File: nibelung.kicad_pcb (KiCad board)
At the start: 2 copper layers, 0 parts

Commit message: Begin preliminary placement
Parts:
- added C1: 0.1uF, Capacitor_SMD:C_0805_2012Metric_Pad1.18x1.45mm_HandSolder, F.Cu at (111.8, 48.3)
- added C2: 10uF, Capacitor_SMD:C_0805_2012Metric_Pad1.18x1.45mm_HandSolder, F.Cu at (87.8, 77.3)
- added C3: 0.1uF, Capacitor_SMD:C_0805_2012Metric_Pad1.18x1.45mm_HandSolder, F.Cu at (116.6, 45.2)
- added C4: 10uF, Capacitor_SMD:C_0805_2012Metric_Pad1.18x1.45mm_HandSolder, F.Cu at (91.6, 72.8)
- added C5: 47nF, Capacitor_SMD:C_0805_2012Metric_Pad1.18x1.45mm_HandSolder, F.Cu at (111.8, 45.2)
- added C6: 10uF, Capacitor_SMD:C_0805_2012Metric_Pad1.18x1.45mm_HandSolder, F.Cu at (60.5, 82.1)
- added C7: 47nF, Capacitor_SMD:C_0805_2012Metric_Pad1.18x1.45mm_HandSolder, F.Cu at (55.7, 82.1)
- added C8: 0.1uF, Capacitor_SMD:C_0805_2012Metric_Pad1.18x1.45mm_HandSolder, F.Cu at (50.9, 82.1)
- added H1: M2, MountingHole:MountingHole_2.2mm_M2, F.Cu at (70.5, 79.1)
- added H2: M2, MountingHole:MountingHole_2.2mm_M2, F.Cu at (76.5, 79.1)
- added H3: M2, MountingHole:MountingHole_2.2mm_M2, F.Cu at (82.4, 79.1)
- added H4: M2, MountingHole:MountingHole_2.2mm_M2, F.Cu at (86.2, 72.9)
- added J2: AudioJack3-TSW, Connector_Audio:Jack_3.5mm_CUI_SJ-3524-SMT_Horizontal, F.Cu at (109.0, 101.6)
- added J3: ScrewTerm_01x08_3.5mm, nibelung:TerminalBlock_Molex_393570008_1x08_P3.50mm_Horizontal, F.Cu at (108.4, 114.6)
- added J4: ScrewTerm_01x08_3.5mm, nibelung:TerminalBlock_Molex_393570008_1x08_P3.50mm_Horizontal, F.Cu at (132.9, 88.6)
- added J5: JST_SH_01x04, Connector_JST:JST_SH_SM04B-SRSS-TB_1x04-1MP_P1.00mm_Horizontal, F.Cu at (135.3, 101.6)
- added J6: JST_SH_01x03, Connector_JST:JST_SH_SM03B-SRSS-TB_1x03-1MP_P1.00mm_Horizontal, B.Cu at (135.3, 104.8)
- added J7: JST_SH_01x03, Connector_JST:JST_SH_SM03B-SRSS-TB_1x03-1MP_P1.00mm_Horizontal, B.Cu at (135.3, 98.4)
- added JP1: SJ2, Jumper:SolderJumper-2_P1.3mm_Bridged_Pad1.0x1.5mm, F.Cu at (111.5, 63.3)
- added JP2: SJ2, Jumper:SolderJumper-2_P1.3mm_Bridged_Pad1.0x1.5mm, F.Cu at (106.5, 70.1)
- added R1: 100, Resistor_SMD:R_0805_2012Metric_Pad1.20x1.40mm_HandSolder, F.Cu at (116.5, 48.2)
- added R10: 100, Resistor_SMD:R_0805_2012Metric_Pad1.20x1.40mm_HandSolder, F.Cu at (116.5, 54.2)
- added R11: 100, Resistor_SMD:R_0805_2012Metric_Pad1.20x1.40mm_HandSolder, F.Cu at (101.9, 66.9)
- added R12: 100, Resistor_SMD:R_0805_2012Metric_Pad1.20x1.40mm_HandSolder, F.Cu at (106.7, 66.9)
- added R13: 100, Resistor_SMD:R_0805_2012Metric_Pad1.20x1.40mm_HandSolder, F.Cu at (97.3, 75.8)
- added R14: 100, Resistor_SMD:R_0805_2012Metric_Pad1.20x1.40mm_HandSolder, F.Cu at (111.7, 60.1)
- added R15: 100, Resistor_SMD:R_0805_2012Metric_Pad1.20x1.40mm_HandSolder, F.Cu at (101.1, 72.8)
- added R16: 100, Resistor_SMD:R_0805_2012Metric_Pad1.20x1.40mm_HandSolder, F.Cu at (111.7, 51.2)
- added R17: 100, Resistor_SMD:R_0805_2012Metric_Pad1.20x1.40mm_HandSolder, F.Cu at (116.5, 57.1)
- added R2: 100k, Resistor_SMD:R_0805_2012Metric_Pad1.20x1.40mm_HandSolder, F.Cu at (116.5, 51.2)
- added R3: 100k, Resistor_SMD:R_0805_2012Metric_Pad1.20x1.40mm_HandSolder, F.Cu at (111.7, 54.2)
- added R4: 100k, Resistor_SMD:R_0805_2012Metric_Pad1.20x1.40mm_HandSolder, F.Cu at (87.8, 80.3)
- added R5: 100k, Resistor_SMD:R_0805_2012Metric_Pad1.20x1.40mm_HandSolder, F.Cu at (96.4, 72.8)
- added R6: 100k, Resistor_SMD:R_0805_2012Metric_Pad1.20x1.40mm_HandSolder, F.Cu at (111.7, 57.1)
- added R7: 47k, Resistor_SMD:R_0805_2012Metric_Pad1.20x1.40mm_HandSolder, F.Cu at (92.6, 75.8)
- added R8: 4.7k, Resistor_SMD:R_0805_2012Metric_Pad1.20x1.40mm_HandSolder, F.Cu at (101.9, 69.8)
- added R9: 4.7k, Resistor_SMD:R_0805_2012Metric_Pad1.20x1.40mm_HandSolder, F.Cu at (92.6, 78.8)
- added U1: 74AHCT245, Package_SO:TSSOP-20_4.4x6.5mm_P0.65mm, B.Cu at (116.3, 101.6)
- added U2: LTC2850IS8, Package_SO:SOIC-8_3.9x4.9mm_P1.27mm, B.Cu at (127.0, 98.3)
- added U3: Teensy4.0, nibelung:Teensy40_Socket, F.Cu at (104.1, 101.6)
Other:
- board outline added: 35.6 x 33 mm

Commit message: Add power connectors
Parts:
- removed the J5 at (135.3, 101.6)
- added J1: JST_PH_01x02, Connector_JST:JST_PH_S2B-PH-SM4-TB_1x02-1MP_P2.00mm_Horizontal, B.Cu at (108.0, 101.6)
- added J3: AudioJack3-TSW, Connector_Audio:Jack_3.5mm_CUI_SJ-3524-SMT_Horizontal, F.Cu at (109.0, 101.6)
- added R18: 1M, Resistor_SMD:R_0805_2012Metric_Pad1.20x1.40mm_HandSolder, F.Cu at (71.2, 103.4)
- J2: value AudioJack3-TSW -> JST_PH_01x02; footprint Connector_Audio:Jack_3.5mm_CUI_SJ-3524-SMT_Horizontal -> Connector_JST:JST_PH_S2B-PH-SM4-TB_1x02-1MP_P2.00mm_Horizontal
- R1: moved to B.Cu
- U1: value 74AHCT245 -> 74HCT245
- moved R1 52.1 mm to (130.8, 98.3), turned to 270 degrees
- moved J2 25.4 mm to (84.2, 96.3), turned to 0 degrees
- moved U1 1.63 mm to (117.3, 102.9)
- moved U2 1.27 mm to (125.7, 98.3)
- moved J6 0.13 mm to (135.3, 104.9)
- moved J7 0.13 mm to (135.3, 98.3)
- renumbered J3 to J4, J4 to J5

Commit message: Adjust for M2.5 mounting holes
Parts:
- removed R8, R9: 4.7k, Resistor_SMD:R_0805_2012Metric_Pad1.20x1.40mm_HandSolder
- H1, H2, H3, H4: value M2 -> M2.5; footprint MountingHole:MountingHole_2.2mm_M2 -> MountingHole:MountingHole_2.7mm_M2.5_Pad_Via
- J4: renamed from J5; value ScrewTerm_01x08_3.5mm -> ScrewTerm_01x08_2.54mm; footprint nibelung:TerminalBlock_Molex_393570008_1x08_P3.50mm_Horizontal -> nibelung:TerminalBlock_Molex_397730008_1x08_P2.54mm_Horizontal
- J5: renamed from J4; value ScrewTerm_01x08_3.5mm -> ScrewTerm_01x08_2.54mm; footprint nibelung:TerminalBlock_Molex_393570008_1x08_P3.50mm_Horizontal -> nibelung:TerminalBlock_Molex_397730008_1x08_P2.54mm_Horizontal
- U2: value LTC2850IS8 -> LTC2850xS8
- moved H4 65.4 mm to (135.3, 116.2)
- moved H2 59.3 mm to (135.3, 87.0)
- moved R18 49.0 mm to (120.1, 104.1), turned to 180 degrees
- moved H3 44.0 mm to (106.0, 116.2)
- moved H1 36.4 mm to (106.0, 87.0)
- moved J4 3.74 mm to (129.5, 87.0)
- moved J5 3.74 mm to (111.8, 116.2)
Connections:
- H1 pad 1: (no net) -> GND
- H2 pad 1: (no net) -> GND
- H3 pad 1: (no net) -> GND
- H4 pad 1: (no net) -> GND
- J4 pad 1: /LED_OUT5 -> /LED_OUT4
- J4 pad 3: /LED_OUT6 -> /LED_OUT3
- J4 pad 5: /LED_OUT7 -> /LED_OUT2
- J4 pad 7: /LED_OUT8 -> /LED_OUT1
- J4 pad 8: GND -> Net-(J4-Pad8)
- J5 pad 1: /LED_OUT1 -> /LED_OUT8
- J5 pad 3: /LED_OUT2 -> /LED_OUT7
- J5 pad 5: /LED_OUT3 -> /LED_OUT6
- J5 pad 7: /LED_OUT4 -> /LED_OUT5
- J5 pad 8: GND -> Net-(J5-Pad8)
- U3 pad 18: Net-(U3-Pad18) -> /RX
- U3 pad 19: Net-(U3-Pad19) -> /TX
- U3 pad 20: /I2C_SDA -> /TXEN
- U3 pad 21: /I2C_SCL -> Net-(U3-Pad21)
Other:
- board size 35.6 x 33 mm -> 35.6 x 35.6 mm

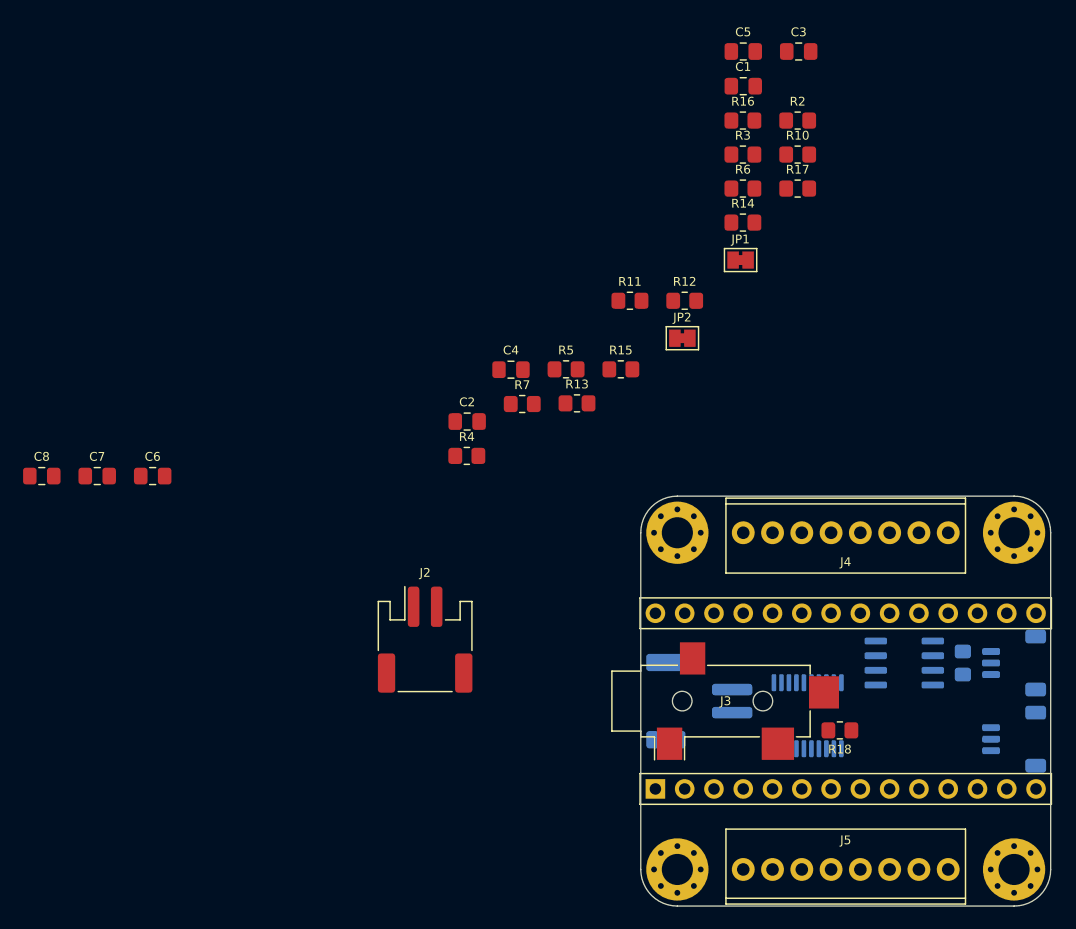
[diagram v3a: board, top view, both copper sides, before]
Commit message: Add indicator LEDs
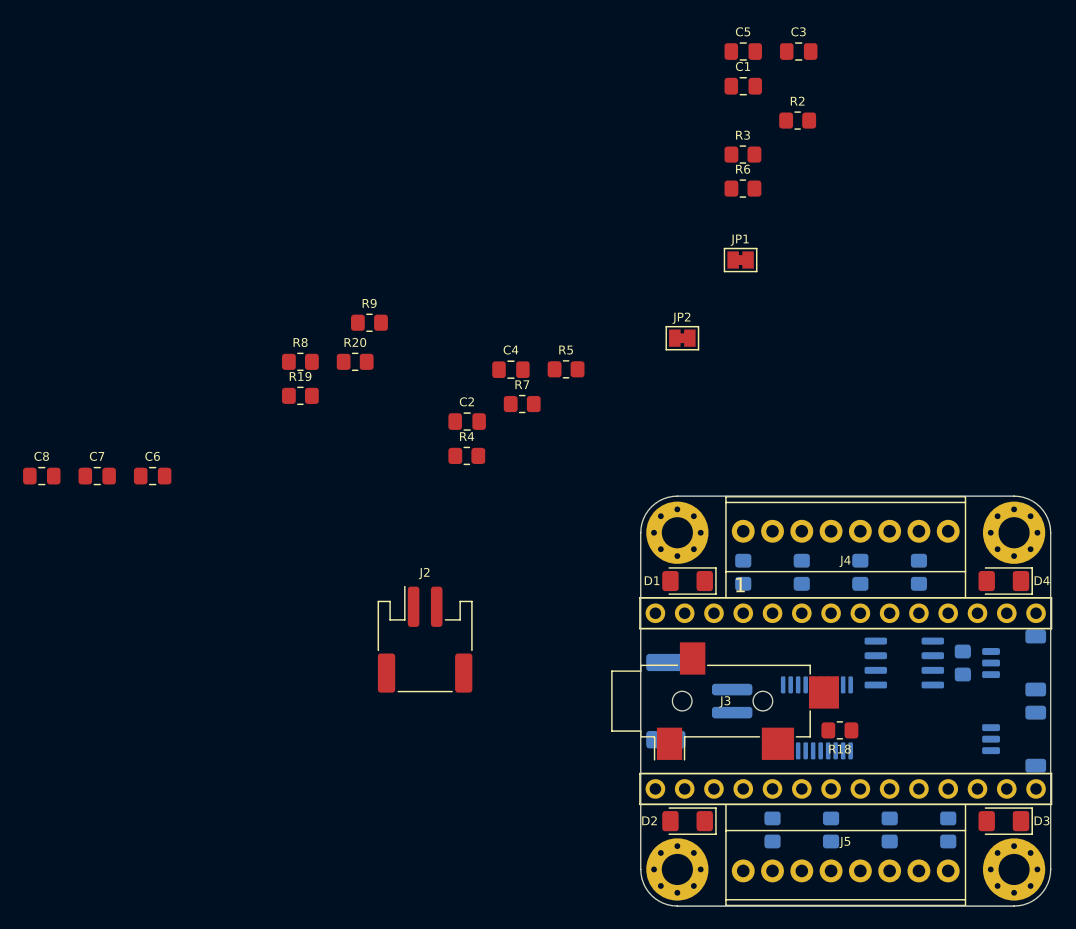
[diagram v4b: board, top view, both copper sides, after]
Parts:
- added D1: RED, LED_SMD:LED_1206_3216Metric_Pad1.42x1.75mm_HandSolder, F.Cu at (106.9, 91.2)
- added D2: AMBER, LED_SMD:LED_1206_3216Metric_Pad1.42x1.75mm_HandSolder, F.Cu at (106.9, 112.0)
- added D3: GREEN, LED_SMD:LED_1206_3216Metric_Pad1.42x1.75mm_HandSolder, F.Cu at (134.4, 112.0)
- added D4: BLUE, LED_SMD:LED_1206_3216Metric_Pad1.42x1.75mm_HandSolder, F.Cu at (134.4, 91.2)
- added R19: 430, Resistor_SMD:R_0805_2012Metric_Pad1.20x1.40mm_HandSolder, F.Cu at (73.3, 75.1)
- added R20: 330, Resistor_SMD:R_0805_2012Metric_Pad1.20x1.40mm_HandSolder, F.Cu at (78.1, 72.2)
- added R8: 10k, Resistor_SMD:R_0805_2012Metric_Pad1.20x1.40mm_HandSolder, F.Cu at (73.3, 72.2)
- added R9: 680, Resistor_SMD:R_0805_2012Metric_Pad1.20x1.40mm_HandSolder, F.Cu at (79.3, 68.8)
- R10, R11, R12, R13, R14, R15, R16, R17: moved to B.Cu
- moved R16 62.0 mm to (119.4, 112.8), turned to 90 degrees
- moved R17 55.7 mm to (114.3, 112.8), turned to 90 degrees
- moved R14 55.6 mm to (129.5, 112.8), turned to 90 degrees
- moved R15 46.3 mm to (124.5, 112.8), turned to 90 degrees
- moved R10 36.5 mm to (111.8, 90.4), turned to 270 degrees
- moved R13 33.1 mm to (127.0, 90.4), turned to 270 degrees
- moved R12 28.1 mm to (121.9, 90.4), turned to 270 degrees
- moved R11 27.9 mm to (116.8, 90.4), turned to 270 degrees
- moved U1 0.82 mm to (118.2, 103.1)
- moved J4 0.13 mm to (129.5, 86.9)
- moved J5 0.13 mm to (111.8, 116.3)
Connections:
- J4 pad 1: /LED_OUT4 -> GND
- J4 pad 2: GND -> /LED_OUT4
- J4 pad 3: /LED_OUT3 -> GND
- J4 pad 4: GND -> /LED_OUT3
- J4 pad 5: /LED_OUT2 -> GND
- J4 pad 6: GND -> /LED_OUT2
- J4 pad 7: /LED_OUT1 -> GND
- J4 pad 8: Net-(J4-Pad8) -> /LED_OUT1
- J5 pad 1: /LED_OUT8 -> GND
- J5 pad 2: GND -> /LED_OUT8
- J5 pad 3: /LED_OUT7 -> GND
- J5 pad 4: GND -> /LED_OUT7
- J5 pad 5: /LED_OUT6 -> GND
- J5 pad 6: GND -> /LED_OUT6
- J5 pad 7: /LED_OUT5 -> GND
- J5 pad 8: Net-(J5-Pad8) -> /LED_OUT5
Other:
- board text added: "1"

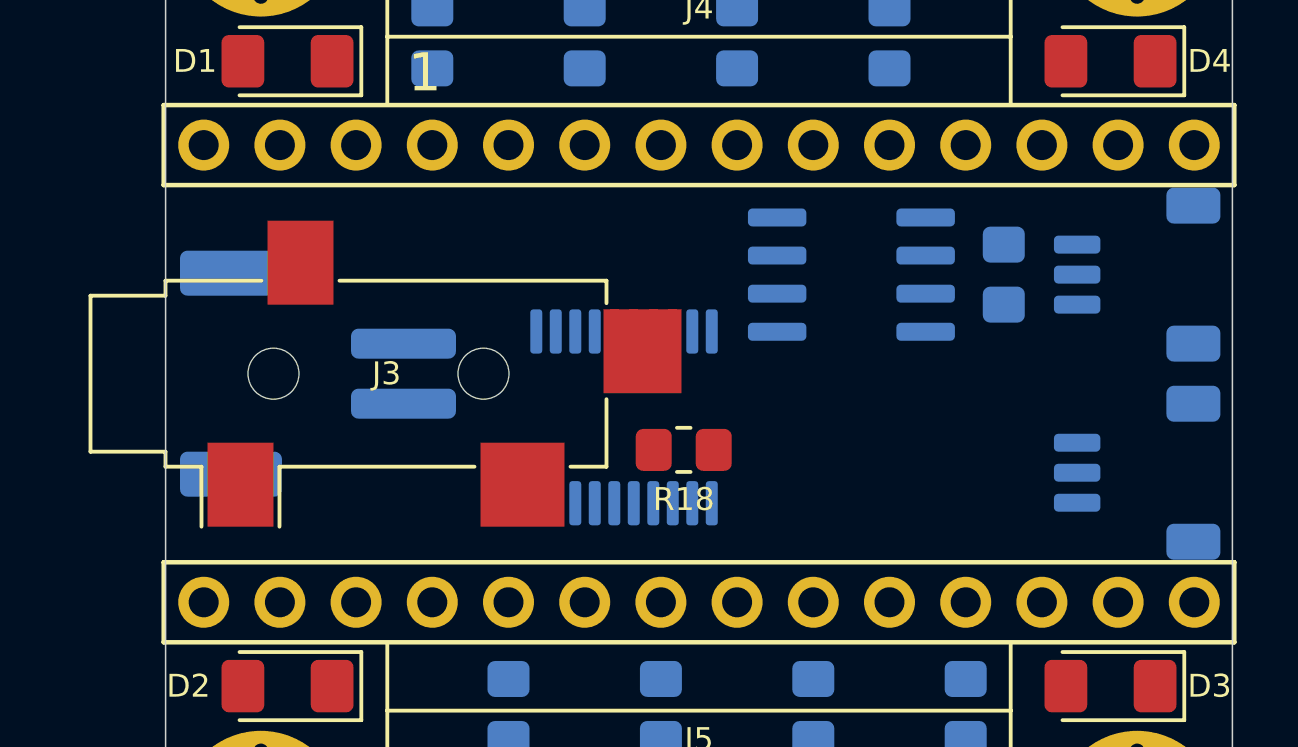
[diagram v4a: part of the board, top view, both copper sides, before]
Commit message: Swap power and RS-485 connector locations
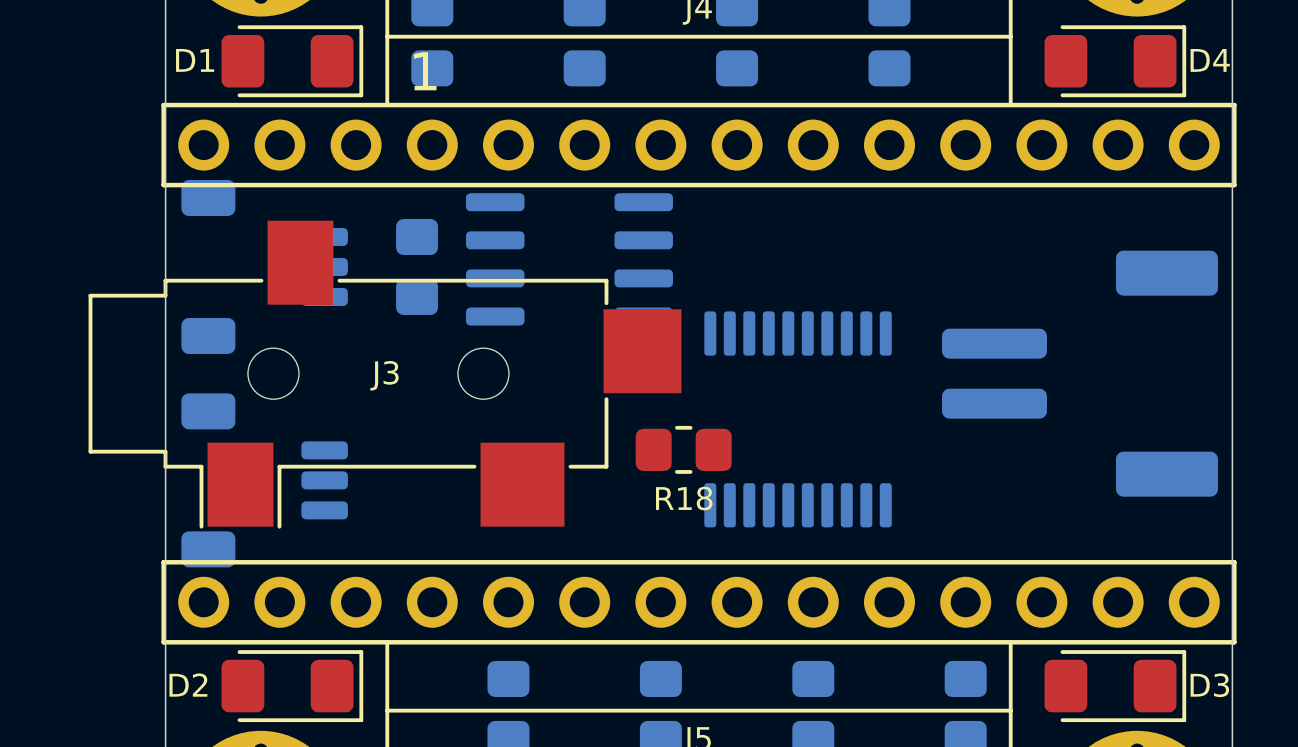
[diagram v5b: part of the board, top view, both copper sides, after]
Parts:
- moved J6 29.9 mm to (106.2, 98.0), turned to 90 degrees
- moved J7 29.9 mm to (106.2, 105.2), turned to 90 degrees
- moved J1 25.4 mm to (133.3, 101.6), turned to 270 degrees
- moved R1 19.6 mm to (111.3, 98.0), turned to 90 degrees
- moved U2 9.41 mm to (116.3, 97.8), turned to 180 degrees
- moved U1 5.80 mm to (124.0, 103.1)
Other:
- board text added: "A"
- board text added: "B"
- board text added: "G"
